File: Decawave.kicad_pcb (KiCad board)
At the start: 4 copper layers, 20 x 40 mm, 47 parts, among them J1 USB_OTG, J2 USART1, J3 PWR, J4 GPIO, SW1 RESET, U1 STM32L443CCTx_u, U2 MCP1700-3302E_SOT23, X1 JTAG-10

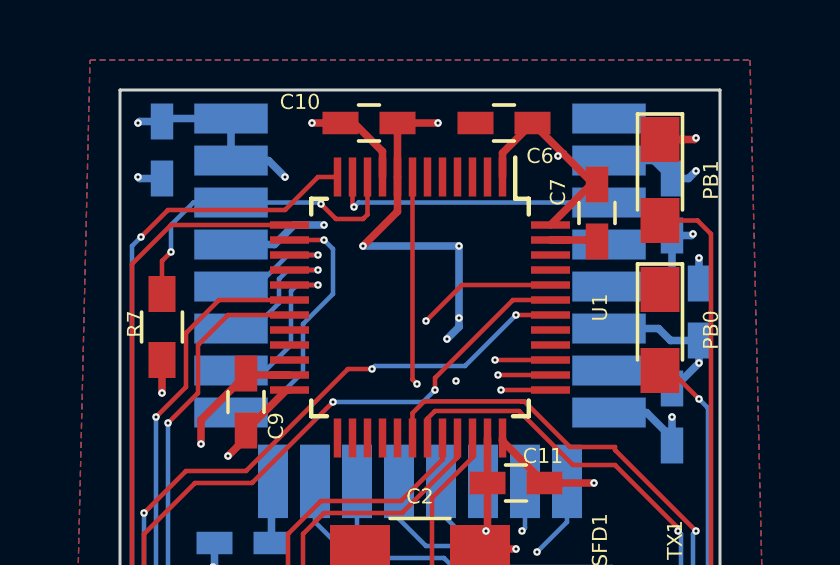
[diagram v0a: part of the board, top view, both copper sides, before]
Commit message: adding 100n Cap for nRST
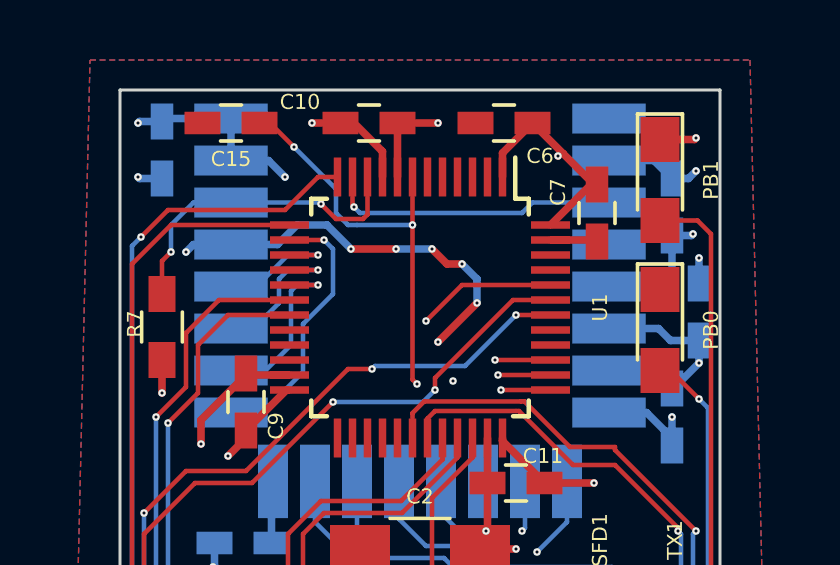
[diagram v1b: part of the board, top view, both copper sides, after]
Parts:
- added C15: 100n, Capacitors_SMD:C_0603_HandSoldering, F.Cu at (63.7, 61.1)
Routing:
- net /nRST: track 33.0 -> 40.0 mm, vias 3 -> 5
- net GND: track 66.4 -> 67.2 mm, vias 24 -> 26

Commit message: add url to gh repo on pcb
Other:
- board text added: "CC-BY-SA 2.0 http://github.com/bastinat0r/ DWM-1000-Adapter-board"
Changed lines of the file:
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@@
     (area 59.949999 59.949999 80.050001 100.050001)
     (thickness 1.6)
-    (drawings 7)
+    (drawings 8)
     (tracks 526)
     (zones 0)
@@
     (34 B.Paste user hide)
     (35 F.Paste user hide)
-    (36 B.SilkS user hide)
-    (37 F.SilkS user hide)
+    (36 B.SilkS user)
+    (37 F.SilkS user)
     (38 B.Mask user hide)
     (39 F.Mask user hide)
@@
     )
   )
+  (gr_text "CC-BY-SA 2.0\nhttp://github.com/bastinat0r/\nDWM-1000-Adapter-board" (at 73.5 82.5) (layer B.SilkS)
+    (effects (font (size 0.5 0.5) (thickness 0.1)) (justify mirror))
+  )
   (dimension 10 (width 0.3) (layer Dwgs.User)

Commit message: Some ground-plane improvements
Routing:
- net GND: track 67.2 -> 69.4 mm, vias 26 -> 27
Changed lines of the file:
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@@
     (thickness 1.6)
     (drawings 8)
-    (tracks 526)
+    (tracks 530)
     (zones 0)
     (modules 48)
@@
   (layers
     (0 F.Cu signal)
-    (1 In1.Cu mixed hide)
-    (2 In2.Cu mixed hide)
-    (31 B.Cu signal hide)
+    (1 In1.Cu mixed)
+    (2 In2.Cu mixed)
+    (31 B.Cu signal)
     (32 B.Adhes user hide)
     (33 F.Adhes user hide)
@@
   (segment (start 68.7 95.6) (end 68.3 96) (width 0.254) (layer F.Cu) (net 1))
   (segment (start 69.9 94.5) (end 69.9 94.9) (width 0.254) (layer B.Cu) (net 1))
+  (segment (start 73.2 75.3) (end 73.4 75.3) (width 0.254) (layer In2.Cu) (net 2))
+  (via (at 73.2 75.3) (size 0.254) (drill 0.1016) (layers F.Cu B.Cu) (net 2))
+  (segment (start 72 75.3) (end 73.2 75.3) (width 0.254) (layer F.Cu) (net 2))
+  (via (at 75.2 74.9) (size 0.254) (drill 0.1016) (layers F.Cu B.Cu) (net 2))
+  (segment (start 73.8 74.9) (end 75.2 74.9) (width 0.254) (layer In2.Cu) (net 2))
+  (segment (start 73.4 75.3) (end 73.8 74.9) (width 0.254) (layer In2.Cu) (net 2))
   (segment (start 70.6 68.4) (end 70.6 69.2) (width 0.254) (layer In2.Cu) (net 2))
   (segment (start 65.2488 65.1512) (end 65.9 64.5) (width 0.254) (layer B.Cu) (net 2))
@@
   (segment (start 68 82.54) (end 68 83.3) (width 0.254) (layer F.Cu) (net 2))
   (via (at 68 83.3) (size 0.254) (drill 0.1016) (layers F.Cu B.Cu) (net 2))
-  (segment (start 72 75.3) (end 73.2 75.3) (width 0.254) (layer F.Cu) (net 2))
-  (via (at 73.2 75.3) (size 0.254) (drill 0.1016) (layers F.Cu B.Cu) (net 2))
   (segment (start 61.4 69) (end 61.4 70.1) (width 0.254) (layer F.Cu) (net 2))
   (via (at 61.4 70.1) (size 0.254) (drill 0.1016) (layers F.Cu B.Cu) (net 2))

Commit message: even more gnd plane improvements
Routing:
- net GND: track 69.4 -> 76.2 mm, vias 27 -> 28
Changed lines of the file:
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@@
     (links 130)
     (no_connects 0)
-    (area 59.949999 59.949999 80.050001 100.050001)
+    (area 58 48.822599 102.85 111.200001)
     (thickness 1.6)
     (drawings 8)
-    (tracks 530)
+    (tracks 537)
     (zones 0)
     (modules 48)
@@
     (34 B.Paste user hide)
     (35 F.Paste user hide)
-    (36 B.SilkS user)
-    (37 F.SilkS user)
+    (36 B.SilkS user hide)
+    (37 F.SilkS user hide)
     (38 B.Mask user hide)
     (39 F.Mask user hide)
@@
     (45 Margin user hide)
     (46 B.CrtYd user hide)
-    (47 F.CrtYd user)
+    (47 F.CrtYd user hide)
     (48 B.Fab user hide)
-    (49 F.Fab user)
+    (49 F.Fab user hide)
   )
   (setup
@@
     (pad_to_mask_clearance 0)
     (aux_axis_origin 0 0)
-    (visible_elements FFFFFE79)
+    (visible_elements FFFFFE19)
     (pcbplotparams
       (layerselection 0x00030_80000001)
@@
   (segment (start 68.7 95.6) (end 68.3 96) (width 0.254) (layer F.Cu) (net 1))
   (segment (start 69.9 94.5) (end 69.9 94.9) (width 0.254) (layer B.Cu) (net 1))
+  (segment (start 74.5 79.2) (end 74.2 78.5) (width 0.254) (layer F.Cu) (net 2))
+  (segment (start 76.8 76.1) (end 74.2 78.5) (width 0.254) (layer In2.Cu) (net 2))
+  (via (at 74.2 78.5) (size 0.254) (drill 0.1016) (layers F.Cu B.Cu) (net 2))
+  (segment (start 78.1 76.1) (end 78.5 76.5) (width 0.254) (layer F.Cu) (net 2))
+  (via (at 78.1 76.1) (size 0.254) (drill 0.1016) (layers F.Cu B.Cu) (net 2))
+  (segment (start 78.1 76.1) (end 76.8 76.1) (width 0.254) (layer In2.Cu) (net 2))
+  (segment (start 62.2 65.4) (end 62.2 65.6) (width 0.254) (layer F.Cu) (net 2))
+  (segment (start 62.4488 65.1512) (end 62.2 65.4) (width 0.254) (layer B.Cu) (net 2))
+  (via (at 62.2 65.4) (size 0.254) (drill 0.1016) (layers F.Cu B.Cu) (net 2))
+  (segment (start 63.7 65.1512) (end 62.4488 65.1512) (width 0.254) (layer B.Cu) (net 2))
+  (segment (start 62.6 66) (end 63 66) (width 0.254) (layer F.Cu) (net 2))
+  (segment (start 62.2 65.6) (end 62.6 66) (width 0.254) (layer F.Cu) (net 2))
   (segment (start 73.2 75.3) (end 73.4 75.3) (width 0.254) (layer In2.Cu) (net 2))
   (via (at 73.2 75.3) (size 0.254) (drill 0.1016) (layers F.Cu B.Cu) (net 2))
@@
   (via (at 71.1 69.7) (size 0.254) (drill 0.1016) (layers F.Cu B.Cu) (net 2))
   (segment (start 70.6 69.2) (end 71.1 69.7) (width 0.254) (layer In2.Cu) (net 2))
-  (segment (start 63.7 65.1512) (end 62.4488 65.1512) (width 0.254) (layer B.Cu) (net 2))
-  (via (at 62.2 65.4) (size 0.254) (drill 0.1016) (layers F.Cu B.Cu) (net 2))
-  (segment (start 62.4488 65.1512) (end 62.2 65.4) (width 0.254) (layer B.Cu) (net 2))
   (segment (start 78.4 62.95) (end 78.95 62.95) (width 0.254) (layer B.Cu) (net 2))
   (via (at 79.2 62.7) (size 0.254) (drill 0.1016) (layers F.Cu B.Cu) (net 2))
@@
   (segment (start 63.7 62.3512) (end 63.7 60.9512) (width 0.254) (layer B.Cu) (net 2))
   (segment (start 78.5 77.15) (end 78.5 76.5) (width 0.254) (layer F.Cu) (net 2))
-  (segment (start 78.5 76.5) (end 78.1 76.1) (width 0.254) (layer F.Cu) (net 2))
-  (via (at 78.1 76.1) (size 0.254) (drill 0.1016) (layers F.Cu B.Cu) (net 2))
   (segment (start 63.7 65.1512) (end 62.6488 65.1512) (width 0.254) (layer B.Cu) (net 2))
   (segment (start 64.2 69.45) (end 64.2 69.5) (width 0.254) (layer F.Cu) (net 2))
@@
   (segment (start 72.5 75.9) (end 76.4 75.9) (width 0.1524) (layer B.Cu) (net 10))
   (segment (start 76.4 75.9) (end 77.9 77.4) (width 0.1524) (layer B.Cu) (net 10))
-  (segment (start 69.3 73.0462) (end 69.3 74.3) (width 0.1524) (layer B.Cu) (net 11))
+  (segment (start 69.3 73.0462) (end 69.3 74.4) (width 0.1524) (layer B.Cu) (net 11))
   (segment (start 73.8 76.3) (end 74.9 77.4) (width 0.1524) (layer B.Cu) (net 11))
   (segment (start 72.2 76.3) (end 73.8 76.3) (width 0.1524) (layer B.Cu) (net 11))
   (segment (start 71.1 75.2) (end 72.2 76.3) (width 0.1524) (layer B.Cu) (net 11))
-  (segment (start 70.2 75.2) (end 71.1 75.2) (width 0.1524) (layer B.Cu) (net 11))
-  (segment (start 69.3 74.3) (end 70.2 75.2) (width 0.1524) (layer B.Cu) (net 11))
-  (segment (start 67.9 73.0462) (end 67.9 75.2) (width 0.1524) (layer B.Cu) (net 12))
+  (segment (start 70.1 75.2) (end 71.1 75.2) (width 0.1524) (layer B.Cu) (net 11))
+  (segment (start 69.3 74.4) (end 70.1 75.2) (width 0.1524) (layer B.Cu) (net 11))
+  (segment (start 67.9 73.0462) (end 67.9 74.4) (width 0.1524) (layer B.Cu) (net 12))
   (segment (start 75.8 78.4) (end 76.4 77.8) (width 0.1524) (layer B.Cu) (net 12))
   (via (at 75.8 78.4) (size 0.254) (drill 0.1016) (layers F.Cu B.Cu) (net 12))
@@
   (via (at 71.8 76.6) (size 0.254) (drill 0.1016) (layers F.Cu B.Cu) (net 12))
   (segment (start 70.8 75.6) (end 71.8 76.6) (width 0.1524) (layer B.Cu) (net 12))
-  (segment (start 68.3 75.6) (end 70.8 75.6) (width 0.1524) (layer B.Cu) (net 12))
-  (segment (start 67.9 75.2) (end 68.3 75.6) (width 0.1524) (layer B.Cu) (net 12))
+  (segment (start 69.1 75.6) (end 70.8 75.6) (width 0.1524) (layer B.Cu) (net 12))
+  (segment (start 67.9 74.4) (end 69.1 75.6) (width 0.1524) (layer B.Cu) (net 12))
   (segment (start 76.4 77.8) (end 76.4 77.4) (width 0.1524) (layer B.Cu) (net 12))
-  (segment (start 73.4 77.4) (end 71.5 77.4) (width 0.1524) (layer B.Cu) (net 13))
+  (segment (start 73.4 77.4) (end 71.9 77.4) (width 0.1524) (layer B.Cu) (net 13))
   (segment (start 66.5 74.4) (end 66.5 73.0462) (width 0.1524) (layer B.Cu) (net 13))
   (segment (start 68.1 76) (end 66.5 74.4) (width 0.1524) (layer B.Cu) (net 13))
-  (segment (start 70.1 76) (end 68.1 76) (width 0.1524) (layer B.Cu) (net 13))
-  (segment (start 71.5 77.4) (end 70.1 76) (width 0.1524) (layer B.Cu) (net 13))
+  (segment (start 70.5 76) (end 68.1 76) (width 0.1524) (layer B.Cu) (net 13))
+  (segment (start 71.9 77.4) (end 70.5 76) (width 0.1524) (layer B.Cu) (net 13))
   (segment (start 63.7 70.75) (end 64.75 70.75) (width 0.1524) (layer B.Cu) (net 14))
   (segment (start 64.75 70.75) (end 66.1 69.4) (width 0.1524) (layer B.Cu) (net 14))
@@
   (via (at 78.6 74.7) (size 0.254) (drill 0.1016) (layers F.Cu B.Cu) (net 22))
   (segment (start 70.25 71.6) (end 70.25 70.95) (width 0.1524) (layer F.Cu) (net 22))
-  (segment (start 76.5 71.9) (end 76.5 72) (width 0.1524) (layer F.Cu) (net 23))
-  (segment (start 73.48 70.38) (end 75 71.9) (width 0.1524) (layer F.Cu) (net 23))
-  (segment (start 75 71.9) (end 76.5 71.9) (width 0.1524) (layer F.Cu) (net 23))
+  (segment (start 76.5 72) (end 76.5 72) (width 0.1524) (layer F.Cu) (net 23))
+  (segment (start 73.48 70.38) (end 75.1 72) (width 0.1524) (layer F.Cu) (net 23))
+  (segment (start 75.1 72) (end 76.5 72) (width 0.1524) (layer F.Cu) (net 23))
   (segment (start 69.75 71.6) (end 69.75 70.77) (width 0.1524) (layer F.Cu) (net 23))
   (segment (start 70.14 70.38) (end 73.37 70.38) (width 0.1524) (layer F.Cu) (net 23))
@@
   (via (at 69.2 88) (size 0.254) (drill 0.1016) (layers F.Cu B.Cu) (net 32))
   (segment (start 65.8 88) (end 69.2 88) (width 0.1524) (layer F.Cu) (net 32))
-  (segment (start 63.5 85.7) (end 65.8 88) (width 0.1524) (layer F.Cu) (net 32))
-  (segment (start 63.5 78.8) (end 63.5 85.7) (width 0.1524) (layer F.Cu) (net 32))
-  (segment (start 61.2 76.5) (end 63.5 78.8) (width 0.1524) (layer F.Cu) (net 32))
+  (segment (start 63.7 85.9) (end 65.8 88) (width 0.1524) (layer F.Cu) (net 32))
+  (segment (start 63.7 78.9) (end 63.7 85.9) (width 0.1524) (layer F.Cu) (net 32))
+  (segment (start 61.2 76.5) (end 63.7 78.9) (width 0.1524) (layer F.Cu) (net 32))
   (via (at 61.2 76.5) (size 0.254) (drill 0.1016) (layers F.Cu B.Cu) (net 32))
   (segment (start 61.2 70.9) (end 61.2 76.5) (width 0.1524) (layer B.Cu) (net 32))

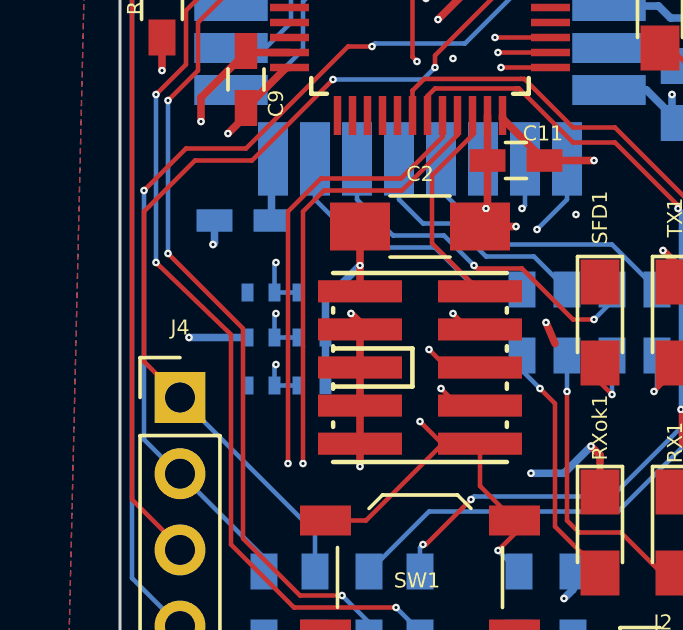
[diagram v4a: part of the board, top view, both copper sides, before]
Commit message: remove unecessary jumpers
* spipol and spipha are internally pulled low by the DWM1000
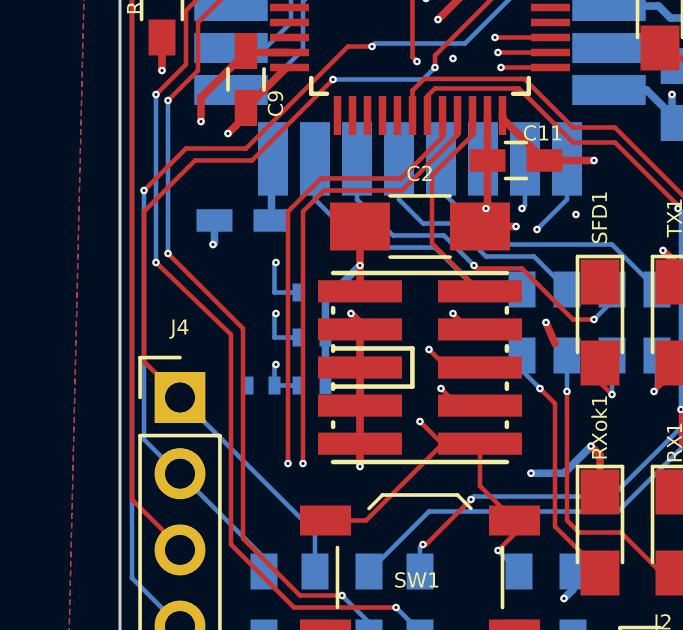
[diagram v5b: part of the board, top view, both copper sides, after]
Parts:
- removed JP1, JP2: Jumper_NC_Small, Resistors_SMD:R_0402
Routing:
- net GND: track 76.2 -> 74.2 mm, vias 28 -> 27
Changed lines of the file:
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@@
 (kicad_pcb (version 4) (host pcbnew 4.0.7)
   (general
-    (links 130)
+    (links 126)
     (no_connects 0)
-    (area 58 48.822599 102.85 111.200001)
+    (area 59.949999 59.949999 80.050001 100.050001)
     (thickness 1.6)
     (drawings 8)
-    (tracks 537)
+    (tracks 535)
     (zones 0)
-    (modules 48)
+    (modules 46)
     (nets 60)
   )
@@
   )
   (module Resistors_SMD:R_0402 placed (layer B.Cu)
-    (at 64.7 77.5)
-    (descr "Resistor SMD 0402, reflow soldering, Vishay (see dcrcw.pdf)")
-    (tags "resistor 0402")
-    (attr smd)
-    (fp_text reference JP1 (at -1.5 -0.1) (layer B.SilkS)
-      (effects (font (size 0.5 0.5) (thickness 0.1)) (justify mirror))
-    )
-    (fp_text value Jumper_NC_Small (at 0 -1.45) (layer B.Fab)
-      (effects (font (size 0.5 0.5) (thickness 0.1)) (justify mirror))
-    )
-    (fp_text user %R (at 0 1.35) (layer B.Fab)
-      (effects (font (size 1 1) (thickness 0.15)) (justify mirror))
-    )
-    (fp_line (start -0.5 -0.25) (end -0.5 0.25) (layer B.Fab) (width 0.1))
-    (fp_line (start 0.5 -0.25) (end -0.5 -0.25) (layer B.Fab) (width 0.1))
-    (fp_line (start 0.5 0.25) (end 0.5 -0.25) (layer B.Fab) (width 0.1))
-    (fp_line (start -0.5 0.25) (end 0.5 0.25) (layer B.Fab) (width 0.1))
-    (fp_line (start 0.25 0.53) (end -0.25 0.53) (layer B.SilkS) (width 0.12))
-    (fp_line (start -0.25 -0.53) (end 0.25 -0.53) (layer B.SilkS) (width 0.12))
-    (fp_line (start -0.8 0.45) (end 0.8 0.45) (layer B.CrtYd) (width 0.05))
-    (fp_line (start -0.8 0.45) (end -0.8 -0.45) (layer B.CrtYd) (width 0.05))
-    (fp_line (start 0.8 -0.45) (end 0.8 0.45) (layer B.CrtYd) (width 0.05))
-    (fp_line (start 0.8 -0.45) (end -0.8 -0.45) (layer B.CrtYd) (width 0.05))
-    (pad 1 smd rect (at -0.45 0) (size 0.4 0.6) (layers B.Cu B.Paste B.Mask)
-      (net 2 GND))
-    (pad 2 smd rect (at 0.45 0) (size 0.4 0.6) (layers B.Cu B.Paste B.Mask)
-      (net 8 /SPIPOL))
-    (model ${KISYS3DMOD}/Resistors_SMD.3dshapes/R_0402.wrl
-      (at (xyz 0 0 0))
-      (scale (xyz 1 1 1))
-      (rotate (xyz 0 0 0))
-    )
-  )
-  (module Resistors_SMD:R_0402 placed (layer B.Cu)
-    (at 64.7 79)
-    (descr "Resistor SMD 0402, reflow soldering, Vishay (see dcrcw.pdf)")
-    (tags "resistor 0402")
-    (attr smd)
-    (fp_text reference JP2 (at -1.4 0) (layer B.SilkS)
-      (effects (font (size 0.5 0.5) (thickness 0.1)) (justify mirror))
-    )
-    (fp_text value Jumper_NC_Small (at 0 -1.45) (layer B.Fab)
-      (effects (font (size 0.5 0.5) (thickness 0.1)) (justify mirror))
-    )
-    (fp_text user %R (at 0 1.35) (layer B.Fab)
-      (effects (font (size 1 1) (thickness 0.15)) (justify mirror))
-    )
-    (fp_line (start -0.5 -0.25) (end -0.5 0.25) (layer B.Fab) (width 0.1))
-    (fp_line (start 0.5 -0.25) (end -0.5 -0.25) (layer B.Fab) (width 0.1))
-    (fp_line (start 0.5 0.25) (end 0.5 -0.25) (layer B.Fab) (width 0.1))
-    (fp_line (start -0.5 0.25) (end 0.5 0.25) (layer B.Fab) (width 0.1))
-    (fp_line (start 0.25 0.53) (end -0.25 0.53) (layer B.SilkS) (width 0.12))
-    (fp_line (start -0.25 -0.53) (end 0.25 -0.53) (layer B.SilkS) (width 0.12))
-    (fp_line (start -0.8 0.45) (end 0.8 0.45) (layer B.CrtYd) (width 0.05))
-    (fp_line (start -0.8 0.45) (end -0.8 -0.45) (layer B.CrtYd) (width 0.05))
-    (fp_line (start 0.8 -0.45) (end 0.8 0.45) (layer B.CrtYd) (width 0.05))
-    (fp_line (start 0.8 -0.45) (end -0.8 -0.45) (layer B.CrtYd) (width 0.05))
-    (pad 1 smd rect (at -0.45 0) (size 0.4 0.6) (layers B.Cu B.Paste B.Mask)
-      (net 2 GND))
-    (pad 2 smd rect (at 0.45 0) (size 0.4 0.6) (layers B.Cu B.Paste B.Mask)
-      (net 7 /SPIPHA))
-    (model ${KISYS3DMOD}/Resistors_SMD.3dshapes/R_0402.wrl
-      (at (xyz 0 0 0))
-      (scale (xyz 1 1 1))
-      (rotate (xyz 0 0 0))
-    )
-  )
-  (module Resistors_SMD:R_0402 placed (layer B.Cu)
     (at 66.4 77.5)
     (descr "Resistor SMD 0402, reflow soldering, Vishay (see dcrcw.pdf)")
@@
   (via (at 75.7 82.625) (size 0.254) (drill 0.1016) (layers F.Cu B.Cu) (net 2))
   (segment (start 76 82.925) (end 75.7 82.625) (width 0.254) (layer F.Cu) (net 2))
-  (segment (start 64.25 79) (end 62.3 79) (width 0.254) (layer B.Cu) (net 2))
-  (via (at 62.3 79) (size 0.254) (drill 0.1016) (layers F.Cu B.Cu) (net 2))
   (segment (start 63.7 60.9512) (end 61.4988 60.9512) (width 0.254) (layer B.Cu) (net 2))
   (segment (start 61.4988 60.9512) (end 61.4 61.05) (width 0.254) (layer B.Cu) (net 2))

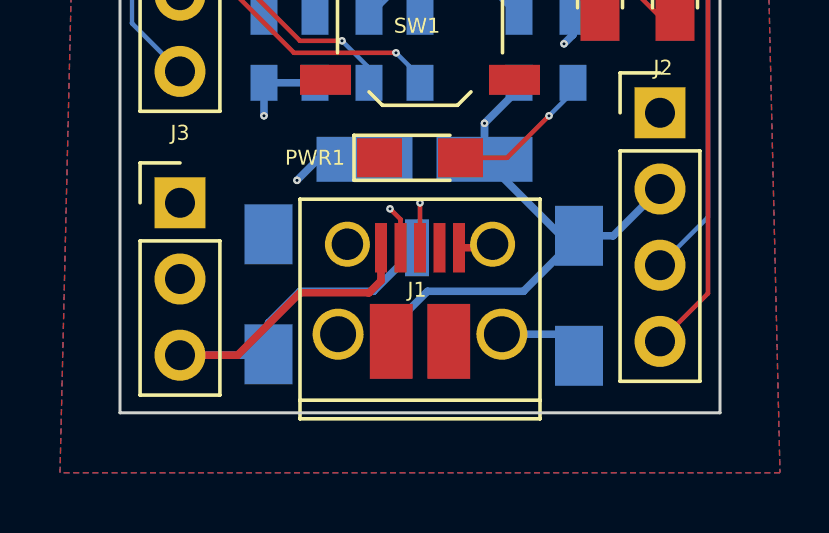
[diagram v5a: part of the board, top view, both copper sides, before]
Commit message: moving usb port closer to the edge
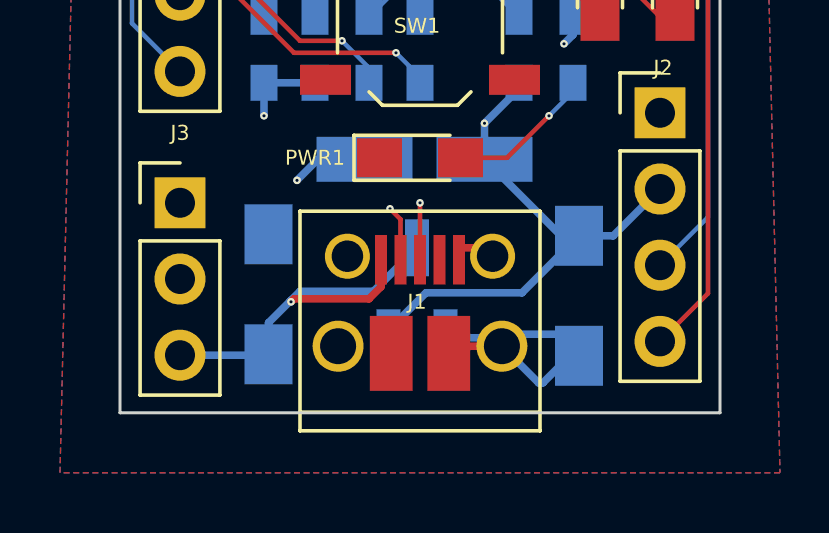
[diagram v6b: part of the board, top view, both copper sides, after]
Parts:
- moved J1 0.40 mm to (70.0, 96.4)
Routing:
- net GND: track 74.2 -> 81.5 mm
- net +5V: track 19.2 -> 15.7 mm, vias 0 -> 1
